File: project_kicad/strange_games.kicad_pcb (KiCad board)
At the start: 2 copper layers, 150 x 150 mm, 116 parts, among them J1 Display, M1 Motor_DC, Q1 Si2302A, Q3 Si2302A, Q4 Q_Photo, SW1 SW_Push, SW10 SW_Push, SW11 SW_Push, SW2 SW_Push, SW3 SW_Push, SW4 SW_Push, SW5 SW_Push, SW6 SW_Push, SW7 SW_Push, SW8 SW_Push, SW9 SW_Push, U1 charge controller, U2 boost converter, U3 LDL1117S33R, U4 ESP32-DEVKIT-V1, U5 TMP112xxDRL, U6 vibrating_sensor, U7 LSM6DS3, U8 MQ-135 gas sensor

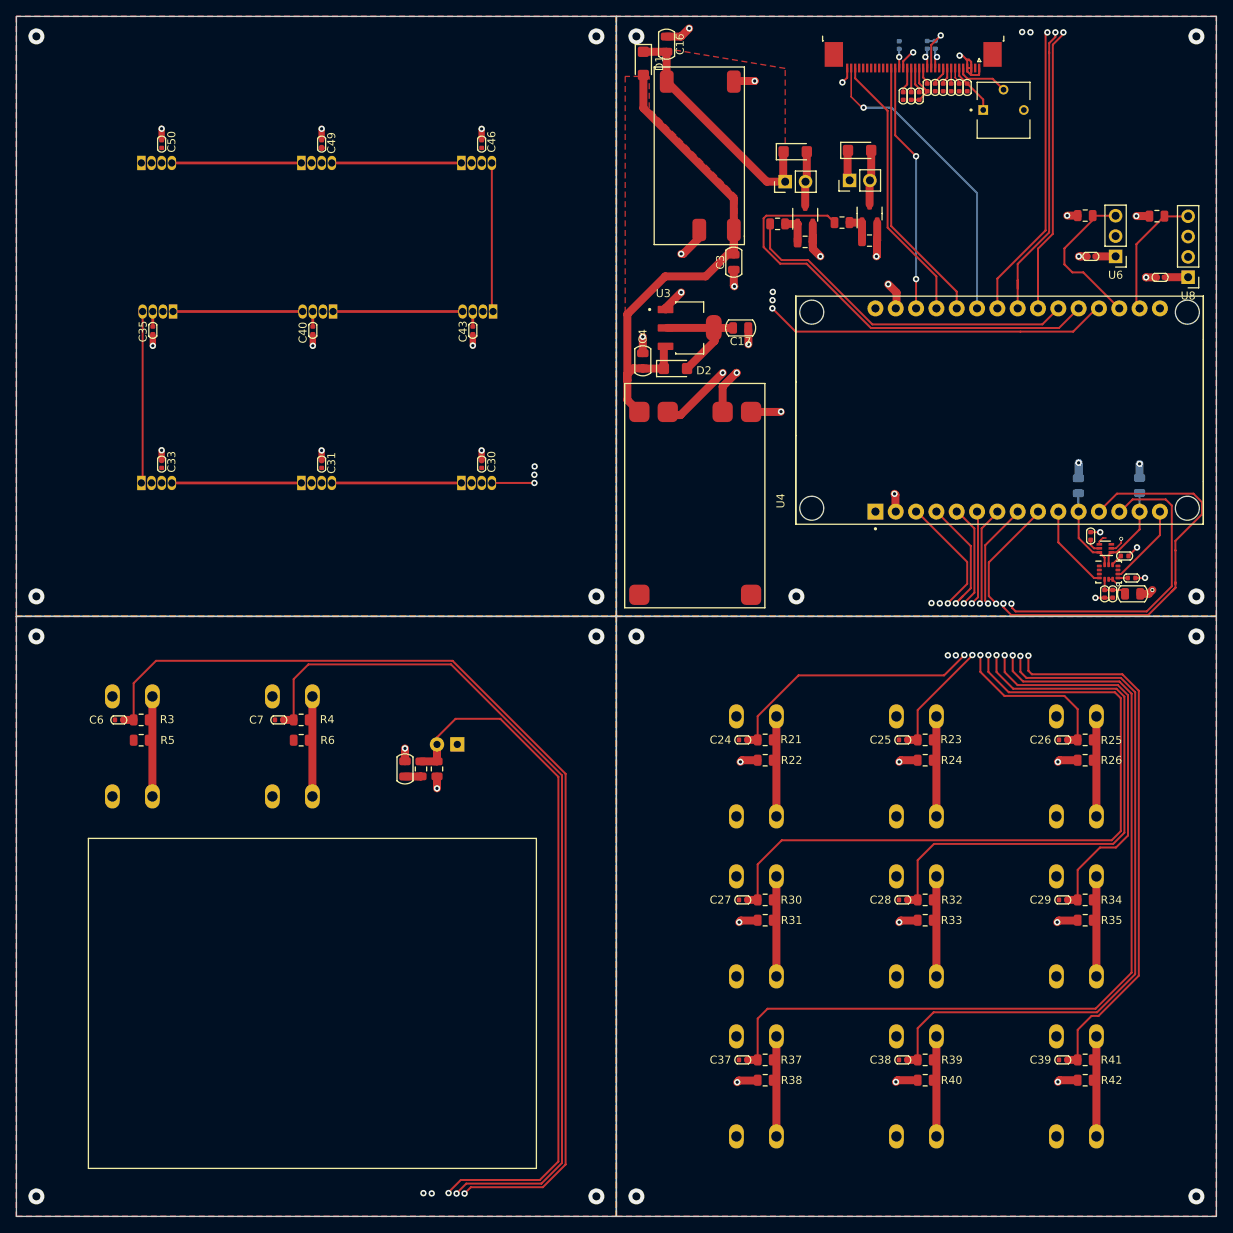
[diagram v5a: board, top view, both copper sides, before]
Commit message: pcb changes
Remade traces: now the are 1mm wide
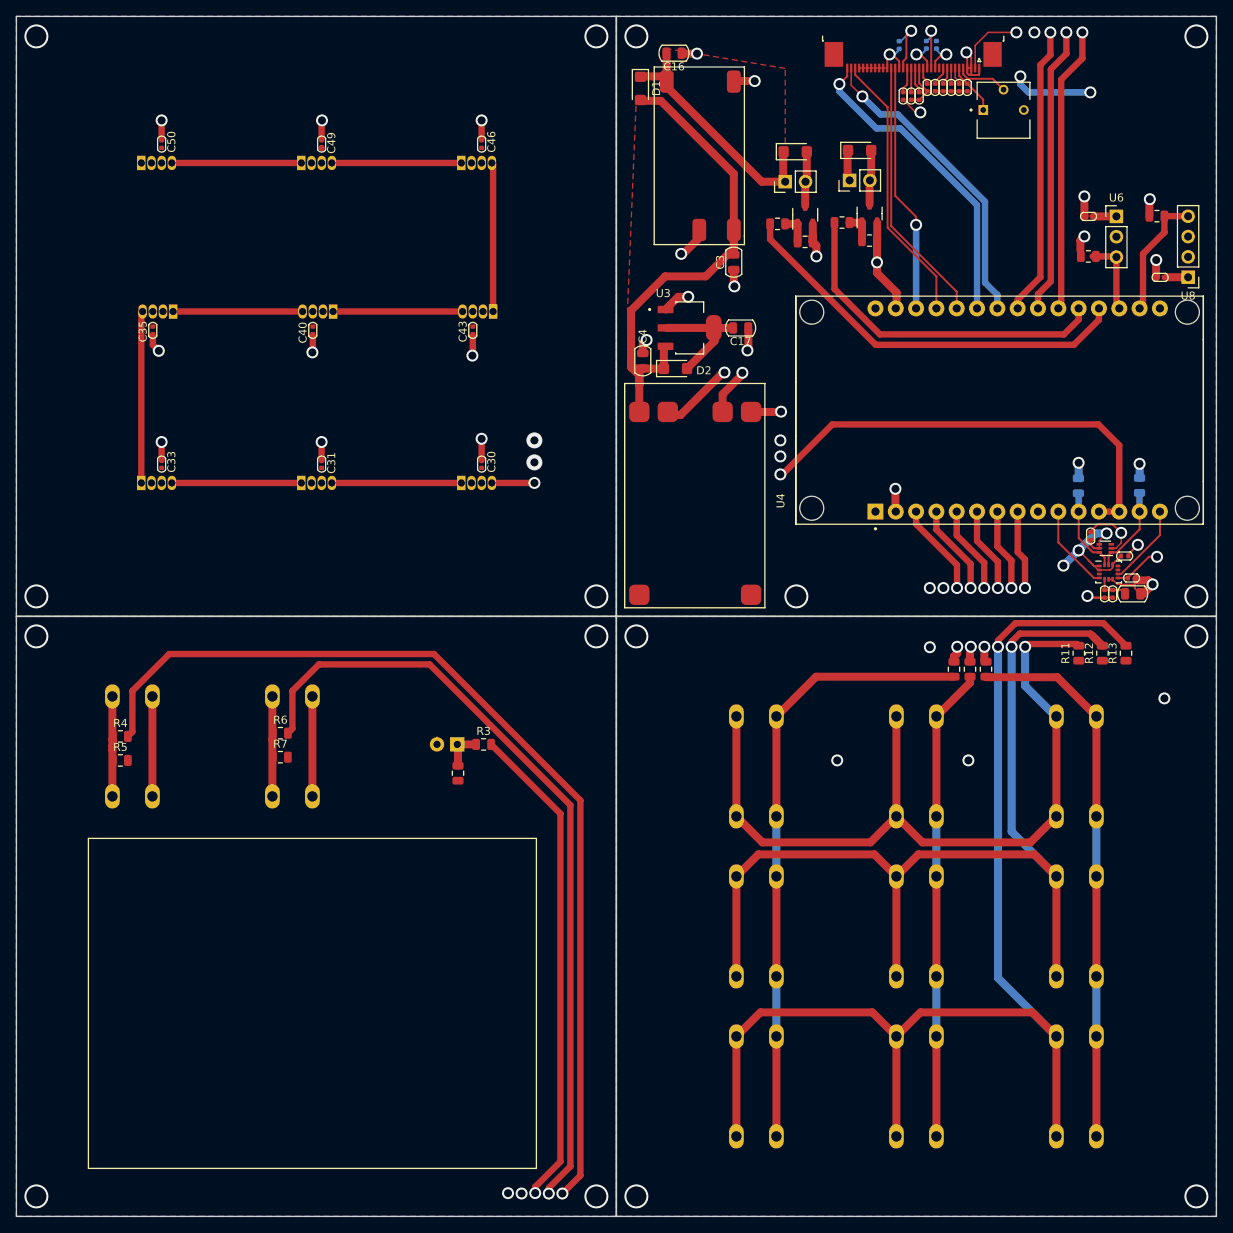
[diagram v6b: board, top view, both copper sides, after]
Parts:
- removed C2: C_Generic, PCM_Capacitor_SMD_AKL:C_0805_2012Metric
- removed C24, C25, C26, C27, C28, C29, C37, C38, C39, C6, C7: C_Generic, PCM_Capacitor_SMD_AKL:C_0402_1005Metric
- removed R21, R23, R25, R28, R30, R32, R34, R37, R39, R41: 330_0805, PCM_4ms_Resistor:R_0805_2012Metric
- removed R22, R24, R26, R31, R33, R35, R38, R40, R42: 10k_0805, PCM_4ms_Resistor:R_0805_2012Metric
- added R10: 330_0805, PCM_4ms_Resistor:R_0805_2012Metric, F.Cu at (250.5, 156.6)
- added R11: 10k_0805, PCM_4ms_Resistor:R_0805_2012Metric, F.Cu at (262.1, 154.6)
- added R12: 10k_0805, PCM_4ms_Resistor:R_0805_2012Metric, F.Cu at (265.1, 154.6)
- added R13: 10k_0805, PCM_4ms_Resistor:R_0805_2012Metric, F.Cu at (268.0, 154.6)
- added R7: 10k_0805, PCM_4ms_Resistor:R_0805_2012Metric, F.Cu at (162.3, 167.6)
- added R8: 330_0805, PCM_4ms_Resistor:R_0805_2012Metric, F.Cu at (246.5, 156.6)
- added R9: 330_0805, PCM_4ms_Resistor:R_0805_2012Metric, F.Cu at (248.5, 156.6)
- R6: value 10k_0805 -> 330_0805
- moved R3 42.9 mm to (187.7, 166.0), turned to 0 degrees
- moved R4 22.7 mm to (142.3, 165.0), turned to 0 degrees
- moved R29 5.12 mm to (263.3, 105.0)
- moved C36 5.01 mm to (263.4, 100.0)
- moved U6 5.00 mm to (266.8, 100.0), turned to 0 degrees
- moved R5 3.62 mm to (142.3, 168.0)
- moved D1 3.15 mm to (207.3, 84.0)
- moved R6 2.74 mm to (162.3, 164.6)
- moved R20 2.68 mm to (184.5, 169.6), turned to -90 degrees
- moved C16 1.46 mm to (211.5, 79.6), turned to 180 degrees
- moved C20 0.15 mm to (244.3, 78.6)
- moved C19 0.10 mm to (243.1, 78.6)
- turned C42 to -90 degrees
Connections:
- C42 pad 1: +3V3 -> GND
- C42 pad 2: GND -> +3V3
- J1 pad 34: GND -> /cs
- J1 pad MP: (no net) -> +3V3
- Q4 pad 1: +3V3 -> Net-(Q4-C)
- Q4 pad 2: PhotoSensor -> GND
- R20 pad 1: GND -> Net-(Q4-C)
- R20 pad 2: PhotoSensor -> +3V3
- R3 pad 1: Net-(R3-Pad1) -> Net-(Q4-C)
- R3 pad 2: B10 -> PhotoSensor
- R4 pad 2: B11 -> B1
- R5 pad 1: GND -> Net-(R4-Pad1)
- R5 pad 2: Net-(R3-Pad1) -> +3V3
- R6 pad 1: GND -> Net-(R6-Pad1)
- R6 pad 2: Net-(R4-Pad1) -> B2
- SW1 pad 1: +3V3 -> Net-(R4-Pad1)
- SW1 pad 2: Net-(R3-Pad1) -> GND
- SW10 pad 1: +3V3 -> Bin3
- SW10 pad 2: Net-(R39-Pad1) -> Net-(R9-Pad1)
- SW11 pad 1: +3V3 -> Bin3
- SW11 pad 2: Net-(R41-Pad1) -> Net-(R10-Pad1)
- SW2 pad 1: +3V3 -> Net-(R6-Pad1)
- SW2 pad 2: Net-(R4-Pad1) -> GND
- SW3 pad 1: +3V3 -> Bin1
- SW3 pad 2: Net-(R21-Pad1) -> Net-(R8-Pad1)
- SW4 pad 1: +3V3 -> Bin1
- SW4 pad 2: Net-(R23-Pad1) -> Net-(R9-Pad1)
- SW5 pad 1: +3V3 -> Bin1
- SW5 pad 2: Net-(R25-Pad1) -> Net-(R10-Pad1)
- SW6 pad 1: +3V3 -> Bin2
- SW6 pad 2: Net-(R30-Pad1) -> Net-(R8-Pad1)
- SW7 pad 1: +3V3 -> Bin2
- SW7 pad 2: Net-(R32-Pad1) -> Net-(R9-Pad1)
- SW8 pad 1: +3V3 -> Bin2
- SW8 pad 2: Net-(R34-Pad1) -> Net-(R10-Pad1)
- SW9 pad 1: +3V3 -> Bin3
- SW9 pad 2: Net-(R37-Pad1) -> Net-(R8-Pad1)
- U4 pad 12: B8 -> Luminodiodes
- U4 pad 13: B9 -> Luminodiodes
- U4 pad 19: Luminodiodes -> Door
- U4 pad 21: Door -> B2
- U4 pad 22: B10 -> B1
- U4 pad 23: B11 -> PhotoSensor
- U4 pad 24: PhotoSensor -> /res
- U4 pad 25: /res -> /cs
- U4 pad 3: B1 -> BOut1
- U4 pad 4: B2 -> BOut2
- U4 pad 5: B3 -> BOut3
- U4 pad 6: B4 -> Bin3
- U4 pad 7: B5 -> Bin2
- U4 pad 8: B6 -> Bin1
- U4 pad 9: B7 -> unconnected-(U4-D18-Pad9)
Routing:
- net B10: track 165.6 -> 0.00 mm, vias 2 -> 0
- net Bin3: track 0.00 -> 163.8 mm, vias 0 -> 2
- net B11: track 147.2 -> 0.00 mm, vias 2 -> 0
- net B8: track 138.8 -> 0.00 mm, vias 2 -> 0
- net Bin2: track 0.00 -> 136.4 mm, vias 0 -> 2
- net B7: track 122.8 -> 0.00 mm, vias 2 -> 0
- net Bin1: track 0.00 -> 110.1 mm, vias 0 -> 2
- net B1: track 48.2 -> 157.8 mm
- net B9: track 107.3 -> 0.00 mm, vias 2 -> 0
- net B2: track 29.4 -> 134.3 mm
- net B4: track 101.2 -> 0.00 mm, vias 2 -> 0
- net B5: track 82.2 -> 0.00 mm, vias 2 -> 0
- net Net-(R8-Pad1): track 0.00 -> 76.8 mm
- net Net-(R10-Pad1): track 0.00 -> 68.4 mm
- net B6: track 62.6 -> 0.00 mm, vias 2 -> 0
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
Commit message: I need to remaster everything
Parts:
- added REF**: NPTH, NPTH, F.Cu at (51.0, 21.0)
- added REF**: NPTH, NPTH, F.Cu at (167.0, 27.2)
- added REF**: NPTH, NPTH, F.Cu at (166.0, 27.2)
- added REF**: NPTH, NPTH, F.Cu at (208.0, 27.0)
- added REF**: NPTH, NPTH, F.Cu at (166.0, 178.8)
- added REF**: NPTH, NPTH, F.Cu at (51.2, 142.0)
- added REF**: NPTH, NPTH, F.Cu at (209.0, 27.0)
- added REF**: NPTH, NPTH, F.Cu at (89.0, 178.8)
- added REF**: NPTH, NPTH, F.Cu at (125.8, 66.0)
- added REF**: NPTH, NPTH, F.Cu at (128.2, 66.0)
- added REF**: NPTH, NPTH, F.Cu at (167.0, 178.8)
- added REF**: NPTH, NPTH, F.Cu at (164.0, 178.8)
- added REF**: NPTH, NPTH, F.Cu at (88.0, 178.8)
- added REF**: NPTH, NPTH, F.Cu at (164.0, 101.8)
- added REF**: NPTH, NPTH, F.Cu at (165.0, 104.2)
- added REF**: NPTH, NPTH, F.Cu at (128.2, 141.0)
- added REF**: NPTH, NPTH, F.Cu at (51.0, 24.0)
- added REF**: NPTH, NPTH, F.Cu at (125.8, 64.0)
- added REF**: NPTH, NPTH, F.Cu at (51.2, 64.0)
- added REF**: Fiducial, Fiducial, B.Cu at (46.0, 184.0)
- added REF**: Fiducial, Fiducial, B.Cu at (208.0, 22.0)
- added REF**: Fiducial, Fiducial, B.Cu at (46.0, 22.0)
- added REF**: NPTH, NPTH, F.Cu at (202.8, 141.0)
- added REF**: NPTH, NPTH, F.Cu at (203.0, 21.0)
- added REF**: NPTH, NPTH, F.Cu at (203.0, 24.0)
- added REF**: NPTH, NPTH, F.Cu at (51.0, 183.0)
- added REF**: NPTH, NPTH, F.Cu at (51.2, 63.0)
- added REF**: NPTH, NPTH, F.Cu at (203.0, 183.0)
- added REF**: NPTH, NPTH, F.Cu at (51.0, 182.0)
- added REF**: NPTH, NPTH, F.Cu at (45.0, 27.0)
- added REF**: NPTH, NPTH, F.Cu at (165.0, 178.8)
- added REF**: NPTH, NPTH, F.Cu at (202.8, 66.0)
- added REF**: NPTH, NPTH, F.Cu at (51.0, 186.0)
- added REF**: NPTH, NPTH, F.Cu at (202.8, 140.0)
- added REF**: NPTH, NPTH, F.Cu at (125.8, 141.0)
- added REF**: NPTH, NPTH, F.Cu at (89.0, 27.2)
- added REF**: NPTH, NPTH, F.Cu at (51.2, 140.0)
- added REF**: NPTH, NPTH, F.Cu at (203.0, 181.0)
- added REF**: NPTH, NPTH, F.Cu at (164.0, 104.2)
- added REF**: NPTH, NPTH, F.Cu at (51.2, 65.0)
- added REF**: NPTH, NPTH, F.Cu at (128.2, 65.0)
- added REF**: NPTH, NPTH, F.Cu at (203.0, 23.0)
- added REF**: NPTH, NPTH, F.Cu at (51.2, 66.0)
- added REF**: NPTH, NPTH, F.Cu at (87.0, 104.2)
- added REF**: NPTH, NPTH, F.Cu at (210.0, 27.0)
- added REF**: NPTH, NPTH, F.Cu at (166.0, 104.2)
- added REF**: NPTH, NPTH, F.Cu at (44.0, 27.0)
- added REF**: NPTH, NPTH, F.Cu at (125.8, 65.0)
- added REF**: NPTH, NPTH, F.Cu at (89.0, 104.2)
- added REF**: NPTH, NPTH, F.Cu at (125.8, 142.0)
- added REF**: NPTH, NPTH, F.Cu at (210.0, 179.0)
- added REF**: NPTH, NPTH, F.Cu at (205.0, 179.0)
- added REF**: NPTH, NPTH, F.Cu at (49.0, 27.0)
- added REF**: NPTH, NPTH, F.Cu at (202.8, 63.0)
- added REF**: NPTH, NPTH, F.Cu at (46.0, 27.0)
- added REF**: NPTH, NPTH, F.Cu at (48.0, 179.0)
- added REF**: NPTH, NPTH, F.Cu at (51.0, 25.0)
- added REF**: NPTH, NPTH, F.Cu at (90.0, 104.2)
- added REF**: NPTH, NPTH, F.Cu at (90.0, 27.2)
- added REF**: NPTH, NPTH, F.Cu at (51.2, 143.0)
- added REF**: NPTH, NPTH, F.Cu at (90.0, 178.8)
- added REF**: NPTH, NPTH, F.Cu at (203.0, 186.0)
- added REF**: NPTH, NPTH, F.Cu at (203.0, 185.0)
- added REF**: NPTH, NPTH, F.Cu at (166.0, 101.8)
- added REF**: NPTH, NPTH, F.Cu at (165.0, 27.2)
- added REF**: NPTH, NPTH, F.Cu at (47.0, 179.0)
- added REF**: NPTH, NPTH, F.Cu at (167.0, 104.2)
- added REF**: Fiducial, Fiducial, F.Cu at (46.0, 184.0)
- added REF**: Fiducial, Fiducial, F.Cu at (208.0, 22.0)
- added REF**: NPTH, NPTH, F.Cu at (90.0, 101.8)
- added REF**: NPTH, NPTH, F.Cu at (203.0, 25.0)
- added REF**: NPTH, NPTH, F.Cu at (88.0, 101.8)
- added REF**: Fiducial, Fiducial, F.Cu at (46.0, 22.0)
- added REF**: NPTH, NPTH, F.Cu at (88.0, 27.2)
- added REF**: NPTH, NPTH, F.Cu at (51.0, 20.0)
- added REF**: NPTH, NPTH, F.Cu at (207.0, 179.0)
- added REF**: NPTH, NPTH, F.Cu at (202.8, 65.0)
- added REF**: NPTH, NPTH, F.Cu at (46.0, 179.0)
- added REF**: NPTH, NPTH, F.Cu at (51.2, 141.0)
- added REF**: NPTH, NPTH, F.Cu at (128.2, 143.0)
- added REF**: NPTH, NPTH, F.Cu at (209.0, 179.0)
- added REF**: NPTH, NPTH, F.Cu at (165.0, 101.8)
- added REF**: NPTH, NPTH, F.Cu at (128.2, 64.0)
- added REF**: NPTH, NPTH, F.Cu at (203.0, 22.0)
- added REF**: NPTH, NPTH, F.Cu at (125.8, 140.0)
- added REF**: NPTH, NPTH, F.Cu at (203.0, 20.0)
- added REF**: NPTH, NPTH, F.Cu at (89.0, 101.8)
- added REF**: NPTH, NPTH, F.Cu at (87.0, 101.8)
- added REF**: NPTH, NPTH, F.Cu at (128.2, 142.0)
- added REF**: NPTH, NPTH, F.Cu at (208.0, 179.0)
- added REF**: NPTH, NPTH, F.Cu at (47.0, 27.0)
- added REF**: NPTH, NPTH, F.Cu at (128.2, 140.0)
- added REF**: NPTH, NPTH, F.Cu at (128.2, 63.0)
- added REF**: NPTH, NPTH, F.Cu at (164.0, 27.2)
- added REF**: NPTH, NPTH, F.Cu at (45.0, 179.0)
- added REF**: NPTH, NPTH, F.Cu at (48.0, 27.0)
- added REF**: NPTH, NPTH, F.Cu at (87.0, 27.2)
- added REF**: NPTH, NPTH, F.Cu at (203.0, 182.0)
- added REF**: NPTH, NPTH, F.Cu at (202.8, 143.0)
- added REF**: NPTH, NPTH, F.Cu at (51.0, 22.0)
- added REF**: NPTH, NPTH, F.Cu at (49.0, 179.0)
- added REF**: NPTH, NPTH, F.Cu at (206.0, 179.0)
- added REF**: NPTH, NPTH, F.Cu at (206.0, 27.0)
- added REF**: NPTH, NPTH, F.Cu at (167.0, 101.8)
- added REF**: NPTH, NPTH, F.Cu at (51.0, 23.0)
- added REF**: NPTH, NPTH, F.Cu at (125.8, 143.0)
- added REF**: NPTH, NPTH, F.Cu at (202.8, 64.0)
- added REF**: NPTH, NPTH, F.Cu at (125.8, 63.0)
- added REF**: NPTH, NPTH, F.Cu at (205.0, 27.0)
- added REF**: NPTH, NPTH, F.Cu at (207.0, 27.0)
- added REF**: NPTH, NPTH, F.Cu at (88.0, 104.2)
- added REF**: NPTH, NPTH, F.Cu at (44.0, 179.0)
- added REF**: NPTH, NPTH, F.Cu at (203.0, 184.0)
- added REF**: NPTH, NPTH, F.Cu at (51.0, 181.0)
- added REF**: NPTH, NPTH, F.Cu at (51.0, 185.0)
- added REF**: NPTH, NPTH, F.Cu at (51.0, 184.0)
- added REF**: NPTH, NPTH, F.Cu at (87.0, 178.8)
- added REF**: NPTH, NPTH, F.Cu at (202.8, 142.0)
- moved Q4 145.9 mm to (106.1, 43.0)
- moved R3 145.9 mm to (109.4, 43.0)
- moved R4 145.9 mm to (64.0, 42.0)
- moved R5 145.9 mm to (64.0, 45.0)
- moved R6 145.9 mm to (84.0, 41.6)
- moved R7 145.9 mm to (84.0, 44.6)
- moved SW1 145.9 mm to (63.0, 37.0)
- moved SW2 145.9 mm to (83.0, 37.0)
- moved R20 145.9 mm to (106.2, 46.6)
- moved C41 90.2 mm to (192.4, 97.2)
- moved R2 90.2 mm to (193.4, 85.6)
- moved R36 90.2 mm to (195.6, 52.0)
- moved D1 90.2 mm to (131.0, 36.0)
- moved D2 90.2 mm to (135.4, 71.0)
- moved D3 90.2 mm to (150.3, 43.9)
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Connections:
- net +12V renamed Board_1-+12V
- net +BATT renamed Board_1-+BATT
- net -BATT renamed Board_1--BATT
- net A0 renamed Board_1-A0
- net CLK renamed Board_1-CLK
- net Door renamed Board_1-Door
- net GasSensor renamed Board_1-GasSensor
- net INT1 renamed Board_1-INT1
- net INT2 renamed Board_1-INT2
- net MOSI renamed Board_1-MOSI
- net Net-(D3-A) renamed Board_1-Net-(D3-A)
- net Net-(D4-A) renamed Board_1-Net-(D4-A)
- net Net-(J1-CAP1+) renamed Board_1-Net-(J1-CAP1+)
- net Net-(J1-CAP1-) renamed Board_1-Net-(J1-CAP1-)
- net Net-(J1-CAP2+) renamed Board_1-Net-(J1-CAP2+)
- net Net-(J1-CAP2-) renamed Board_1-Net-(J1-CAP2-)
- net Net-(J1-CAP3+) renamed Board_1-Net-(J1-CAP3+)
- net Net-(J1-CAP4+) renamed Board_1-Net-(J1-CAP4+)
- net Net-(J1-CAP5+) renamed Board_1-Net-(J1-CAP5+)
- net Net-(J1-V0) renamed Board_1-Net-(J1-V0)
- net Net-(J1-V1) renamed Board_1-Net-(J1-V1)
- net Net-(J1-V2) renamed Board_1-Net-(J1-V2)
- net Net-(J1-V3) renamed Board_1-Net-(J1-V3)
- net Net-(J1-V4) renamed Board_1-Net-(J1-V4)
- net Net-(J1-VR) renamed Board_1-Net-(J1-VR)
- net Net-(J1-Vout) renamed Board_1-Net-(J1-Vout)
- net Net-(Q1-G) renamed Board_1-Net-(Q1-G)
- net Net-(Q3-G) renamed Board_1-Net-(Q3-G)
- net SCL renamed Board_1-SCL
- net SDA renamed Board_1-SDA
- net VDC renamed Board_1-VDC
- net VibrationMotor renamed Board_1-VibrationMotor
- net VibrationSensor renamed Board_1-VibrationSensor
- net /cs renamed Board_1-/cs
- net /res renamed Board_1-/res
- C1 pad 1: GND -> Board_1-GND
- C1 pad 2: +3V3 -> Board_1-+3V3
- C11 pad 1: +3V3 -> Board_1-+3V3
- C12 pad 1: +3V3 -> Board_1-+3V3
- C13 pad 1: +3V3 -> Board_1-+3V3
- C14 pad 1: +3V3 -> Board_1-+3V3
- C15 pad 1: +3V3 -> Board_1-+3V3
- C16 pad 1: GND -> Board_1-GND
- C17 pad 1: GND -> Board_1-GND
- C17 pad 2: +3V3 -> Board_1-+3V3
- C23 pad 2: GND -> Board_1-GND
- C3 pad 1: GND -> Board_1-GND
- C30 pad 1: GND -> (no net)
- C30 pad 2: +3V3 -> (no net)
- C31 pad 1: +3V3 -> (no net)
- C31 pad 2: GND -> (no net)
- C32 pad 1: GND -> Board_1-GND
- C32 pad 2: +3V3 -> Board_1-+3V3
- C33 pad 1: GND -> (no net)
- C33 pad 2: +3V3 -> (no net)
- C34 pad 1: +3V3 -> Board_1-+3V3
- C34 pad 2: GND -> Board_1-GND
- C35 pad 1: +3V3 -> (no net)
- C35 pad 2: GND -> (no net)
- C36 pad 1: GND -> Board_1-GND
- C36 pad 2: +3V3 -> Board_1-+3V3
- C4 pad 1: GND -> Board_1-GND
- C40 pad 1: GND -> (no net)
- C40 pad 2: +3V3 -> (no net)
- C41 pad 1: GND -> Board_1-GND
- C41 pad 2: +3V3 -> Board_1-+3V3
- C42 pad 1: GND -> Board_1-GND
- C42 pad 2: +3V3 -> Board_1-+3V3
- C43 pad 1: +3V3 -> (no net)
- C43 pad 2: GND -> (no net)
- C44 pad 1: GND -> Board_1-GND
- C44 pad 2: +3V3 -> Board_1-+3V3
- C46 pad 1: GND -> (no net)
- C46 pad 2: +3V3 -> (no net)
- C47 pad 1: GND -> Board_1-GND
- C47 pad 2: +3V3 -> Board_1-+3V3
- C48 pad 1: GND -> Board_1-GND
- C48 pad 2: +3V3 -> Board_1-+3V3
- C49 pad 1: +3V3 -> (no net)
- C49 pad 2: GND -> (no net)
- C50 pad 1: GND -> (no net)
- C50 pad 2: +3V3 -> (no net)
- D10 pad 1: Net-(D10-DO) -> (no net)
- D10 pad 2: GND -> (no net)
- D10 pad 3: +3V3 -> (no net)
- D10 pad 4: Net-(D10-DI) -> (no net)
- D11 pad 1: Net-(D11-DO) -> (no net)
- D11 pad 2: GND -> (no net)
- D11 pad 3: +3V3 -> (no net)
- D11 pad 4: Net-(D10-DO) -> (no net)
- D12 pad 1: Net-(D12-DO) -> (no net)
- D12 pad 2: GND -> (no net)
- D12 pad 3: +3V3 -> (no net)
- D12 pad 4: Net-(D11-DO) -> (no net)
- D13 pad 1: unconnected-(D13-DO-Pad1) -> (no net)
- D13 pad 2: GND -> (no net)
- D13 pad 3: +3V3 -> (no net)
- D13 pad 4: Net-(D12-DO) -> (no net)
- D2 pad 2: +3V3 -> Board_1-+3V3
- D4 pad 1: +3V3 -> Board_1-+3V3
- D5 pad 1: Net-(D5-DO) -> (no net)
- D5 pad 2: GND -> (no net)
- D5 pad 3: +3V3 -> (no net)
- D5 pad 4: Luminodiodes -> (no net)
- D6 pad 1: Net-(D6-DO) -> (no net)
- D6 pad 2: GND -> (no net)
- D6 pad 3: +3V3 -> (no net)
- D6 pad 4: Net-(D5-DO) -> (no net)
- D7 pad 1: Net-(D7-DO) -> (no net)
- D7 pad 2: GND -> (no net)
- D7 pad 3: +3V3 -> (no net)
- D7 pad 4: Net-(D6-DO) -> (no net)
- D8 pad 1: Net-(D8-DO) -> (no net)
- D8 pad 2: GND -> (no net)
- D8 pad 3: +3V3 -> (no net)
- D8 pad 4: Net-(D7-DO) -> (no net)
- D9 pad 1: Net-(D10-DI) -> (no net)
- D9 pad 2: GND -> (no net)
- D9 pad 3: +3V3 -> (no net)
- D9 pad 4: Net-(D8-DO) -> (no net)
- J1 pad 1: GND -> Board_1-GND
- J1 pad 11: unconnected-(J1-VRS-Pad11) -> Board_1-unconnected-(J1-VRS-Pad11)
- J1 pad 2: +3V3 -> Board_1-+3V3
- J1 pad 20: GND -> Board_1-GND
- J1 pad 21: +3V3 -> Board_1-+3V3
- J1 pad 24: +3V3 -> Board_1-+3V3
- J1 pad 25: +3V3 -> Board_1-+3V3
- J1 pad 26: +3V3 -> Board_1-+3V3
- J1 pad 27: +3V3 -> Board_1-+3V3
- J1 pad 28: +3V3 -> Board_1-+3V3
- J1 pad 29: +3V3 -> Board_1-+3V3
- J1 pad 3: GND -> Board_1-GND
- J1 pad 30: +3V3 -> Board_1-+3V3
- J1 pad 31: +3V3 -> Board_1-+3V3
- J1 pad 4: GND -> Board_1-GND
- J1 pad MP: +3V3 -> Board_1-+3V3
- M1 pad 1: +3V3 -> Board_1-+3V3
- Q1 pad 2: GND -> Board_1-GND
- Q3 pad 2: GND -> Board_1-GND
- Q4 pad 1: Net-(Q4-C) -> (no net)
- Q4 pad 2: GND -> (no net)
- R1 pad 2: +3V3 -> Board_1-+3V3
- R10 pad 1: Net-(R10-Pad1) -> (no net)
- R10 pad 2: BOut3 -> (no net)
- R11 pad 1: GND -> (no net)
- R11 pad 2: Bin1 -> (no net)
- R12 pad 1: GND -> (no net)
- R12 pad 2: Bin2 -> (no net)
- R13 pad 1: GND -> (no net)
- R13 pad 2: Bin3 -> (no net)
- R16 pad 1: GND -> Board_1-GND
- R18 pad 1: GND -> Board_1-GND
- R2 pad 2: +3V3 -> Board_1-+3V3
- R20 pad 1: Net-(Q4-C) -> (no net)
- R20 pad 2: +3V3 -> (no net)
- R29 pad 1: GND -> Board_1-GND
- R3 pad 1: Net-(Q4-C) -> (no net)
- R3 pad 2: PhotoSensor -> (no net)
- R36 pad 1: GND -> Board_1-GND
- R4 pad 1: Net-(R4-Pad1) -> (no net)
- R4 pad 2: B1 -> (no net)
- R5 pad 1: Net-(R4-Pad1) -> (no net)
- R5 pad 2: +3V3 -> (no net)
- R6 pad 1: Net-(R6-Pad1) -> (no net)
- R6 pad 2: B2 -> (no net)
- R7 pad 1: Net-(R6-Pad1) -> (no net)
- R7 pad 2: +3V3 -> (no net)
- R8 pad 1: Net-(R8-Pad1) -> (no net)
- R8 pad 2: BOut1 -> (no net)
- R9 pad 1: Net-(R9-Pad1) -> (no net)
- R9 pad 2: BOut2 -> (no net)
- RV1 pad 3: GND -> Board_1-GND
- SW1 pad 1: Net-(R4-Pad1) -> (no net)
- SW1 pad 2: GND -> (no net)
- SW10 pad 1: Bin3 -> (no net)
- SW10 pad 2: Net-(R9-Pad1) -> (no net)
- SW11 pad 1: Bin3 -> (no net)
- SW11 pad 2: Net-(R10-Pad1) -> (no net)
- SW2 pad 1: Net-(R6-Pad1) -> (no net)
- SW2 pad 2: GND -> (no net)
- SW3 pad 1: Bin1 -> (no net)
- SW3 pad 2: Net-(R8-Pad1) -> (no net)
- SW4 pad 1: Bin1 -> (no net)
- SW4 pad 2: Net-(R9-Pad1) -> (no net)
- SW5 pad 1: Bin1 -> (no net)
- SW5 pad 2: Net-(R10-Pad1) -> (no net)
- SW6 pad 1: Bin2 -> (no net)
- SW6 pad 2: Net-(R8-Pad1) -> (no net)
- SW7 pad 1: Bin2 -> (no net)
- SW7 pad 2: Net-(R9-Pad1) -> (no net)
- SW8 pad 1: Bin2 -> (no net)
- SW8 pad 2: Net-(R10-Pad1) -> (no net)
- SW9 pad 1: Bin3 -> (no net)
- SW9 pad 2: Net-(R8-Pad1) -> (no net)
- U1 pad 1: unconnected-(U1-+-Pad1) -> Board_1-unconnected-(U1-+-Pad1)
- U1 pad 2: unconnected-(U1---Pad2) -> Board_1-unconnected-(U1---Pad2)
- U1 pad 6: GND -> Board_1-GND
- U2 pad 2: GND -> Board_1-GND
- U2 pad 4: GND -> Board_1-GND
- U3 pad 1: GND -> Board_1-GND
- U3 pad 2: +3V3 -> Board_1-+3V3
- U3 pad 4: +3V3 -> Board_1-+3V3
- U4 pad 1: +3V3 -> Board_1-+3V3
- U4 pad 12: Luminodiodes -> Board_1-Luminodiodes
- U4 pad 13: Luminodiodes -> Board_1-Luminodiodes
- U4 pad 16: +3V3 -> Board_1-+3V3
- U4 pad 2: GND -> Board_1-GND
- U4 pad 21: B2 -> Board_1-B2
- U4 pad 22: B1 -> Board_1-B1
- U4 pad 23: PhotoSensor -> Board_1-PhotoSensor
- U4 pad 29: GND -> Board_1-GND
- U4 pad 3: BOut1 -> Board_1-BOut1
- U4 pad 30: unconnected-(U4-VIN-Pad30) -> Board_1-unconnected-(U4-VIN-Pad30)
- U4 pad 4: BOut2 -> Board_1-BOut2
- U4 pad 5: BOut3 -> Board_1-BOut3
- U4 pad 6: Bin3 -> Board_1-Bin3
- U4 pad 7: Bin2 -> Board_1-Bin2
- U4 pad 8: Bin1 -> Board_1-Bin1
- U4 pad 9: unconnected-(U4-D18-Pad9) -> Board_1-unconnected-(U4-D18-Pad9)
- U5 pad 2: GND -> Board_1-GND
- U5 pad 3: unconnected-(U5-ALERT-Pad3) -> Board_1-unconnected-(U5-ALERT-Pad3)
- U5 pad 4: +3V3 -> Board_1-+3V3
- U5 pad 5: +3V3 -> Board_1-+3V3
- U6 pad 1: +3V3 -> Board_1-+3V3
- U6 pad 2: GND -> Board_1-GND
- U7 pad 1: +3V3 -> Board_1-+3V3
- U7 pad 10: unconnected-(U7-NC-Pad10) -> Board_1-unconnected-(U7-NC-Pad10)
- U7 pad 11: unconnected-(U7-NC-Pad11) -> Board_1-unconnected-(U7-NC-Pad11)
- U7 pad 12: +3V3 -> Board_1-+3V3
- U7 pad 2: +3V3 -> Board_1-+3V3
- U7 pad 3: +3V3 -> Board_1-+3V3
- U7 pad 5: +3V3 -> Board_1-+3V3
- U7 pad 6: GND -> Board_1-GND
- U7 pad 7: GND -> Board_1-GND
- U7 pad 8: +3V3 -> Board_1-+3V3
- U8 pad 1: +3V3 -> Board_1-+3V3
- U8 pad 2: GND -> Board_1-GND
- U8 pad 3: unconnected-(U8-AO-Pad3) -> Board_1-unconnected-(U8-AO-Pad3)
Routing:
- net (no net): track 0.00 -> 1094.6 mm, vias 16 -> 43
- net Bin3: track 163.8 -> 0.00 mm, vias 2 -> 0
- net B1: track 157.8 -> 0.00 mm, vias 2 -> 0
- net GND: track 137.0 -> 0.00 mm, vias 40 -> 0
- net Bin2: track 136.4 -> 0.00 mm, vias 2 -> 0
- net B2: track 134.3 -> 0.00 mm, vias 2 -> 0
- net Bin1: track 110.1 -> 0.00 mm, vias 2 -> 0
- net Board_1-+3V3: track 0.00 -> 105.8 mm, vias 0 -> 14
- net PhotoSensor: track 97.4 -> 0.00 mm, vias 2 -> 0
- net +3V3: track 91.2 -> 0.00 mm, vias 14 -> 0
- net Board_1-GND: track 0.00 -> 90.3 mm, vias 0 -> 25
- net Net-(R8-Pad1): track 76.8 -> 0.00 mm
- net Net-(R10-Pad1): track 68.4 -> 0.00 mm
- net Luminodiodes: track 62.3 -> 0.00 mm, vias 2 -> 0
- net Net-(R9-Pad1): track 59.2 -> 0.00 mm
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- added copper zone on B.Cu, net (none)
- added copper zone on F.Cu, net (none)
- added copper zone on F.Cu, net Board_1-+3V3
- added copper zone on B.Cu, net Board_1-GND
- added copper zone on F.Cu, net Board_1-GND
- removed copper zone on F.Cu, net +3V3
- removed copper zone on B.Cu, net GND
- removed copper zone on F.Cu, net GND
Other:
- board size 150 x 150 mm -> 166 x 166 mm
